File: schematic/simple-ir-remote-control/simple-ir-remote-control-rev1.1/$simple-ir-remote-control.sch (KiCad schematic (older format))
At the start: 24 parts, among them K1 CONN_3, P1 CONN_1, P2 CONN_1, P3 CONN_1, P4 CONN_1, P5 CONN_5, P6 CONN_4, P7 CONN_5X2, P8 CONN_10, P9 CONN_2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

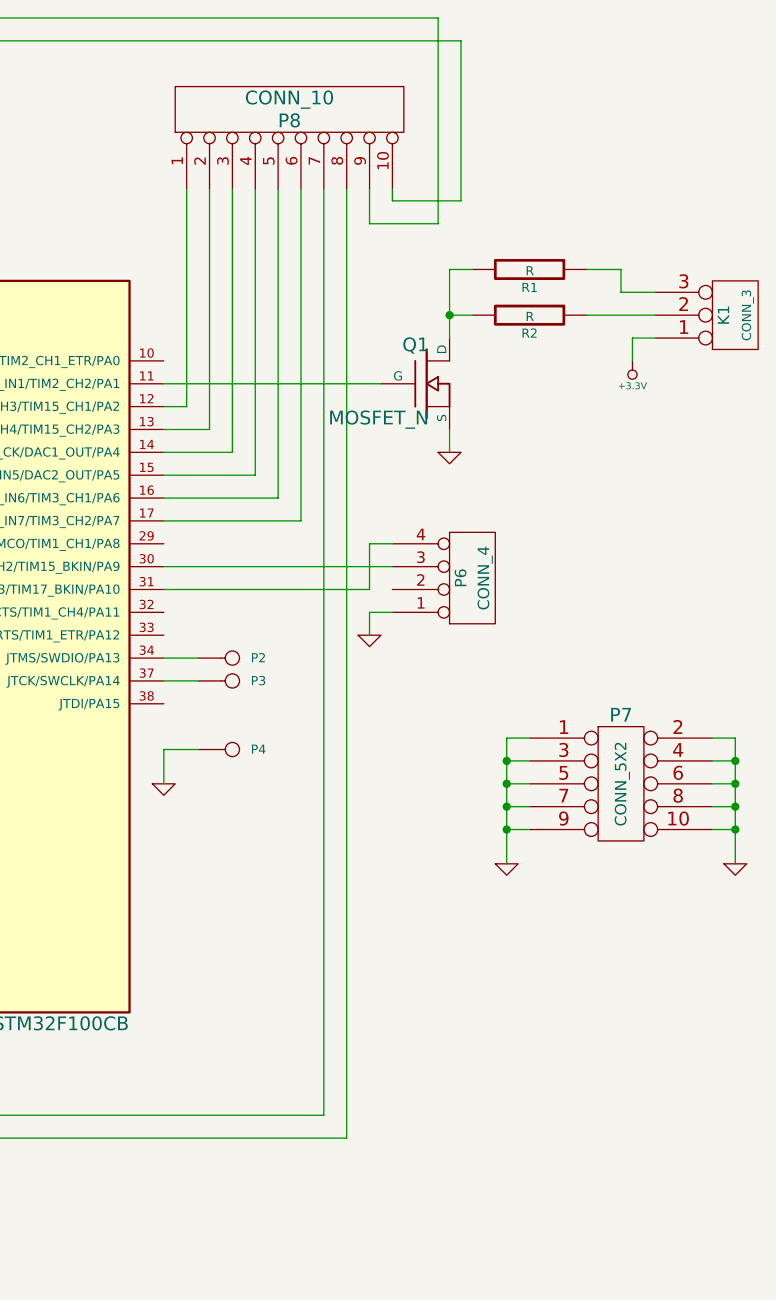
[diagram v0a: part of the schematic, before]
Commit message: Simple irrc rev 1.1 done - better design for manual producing
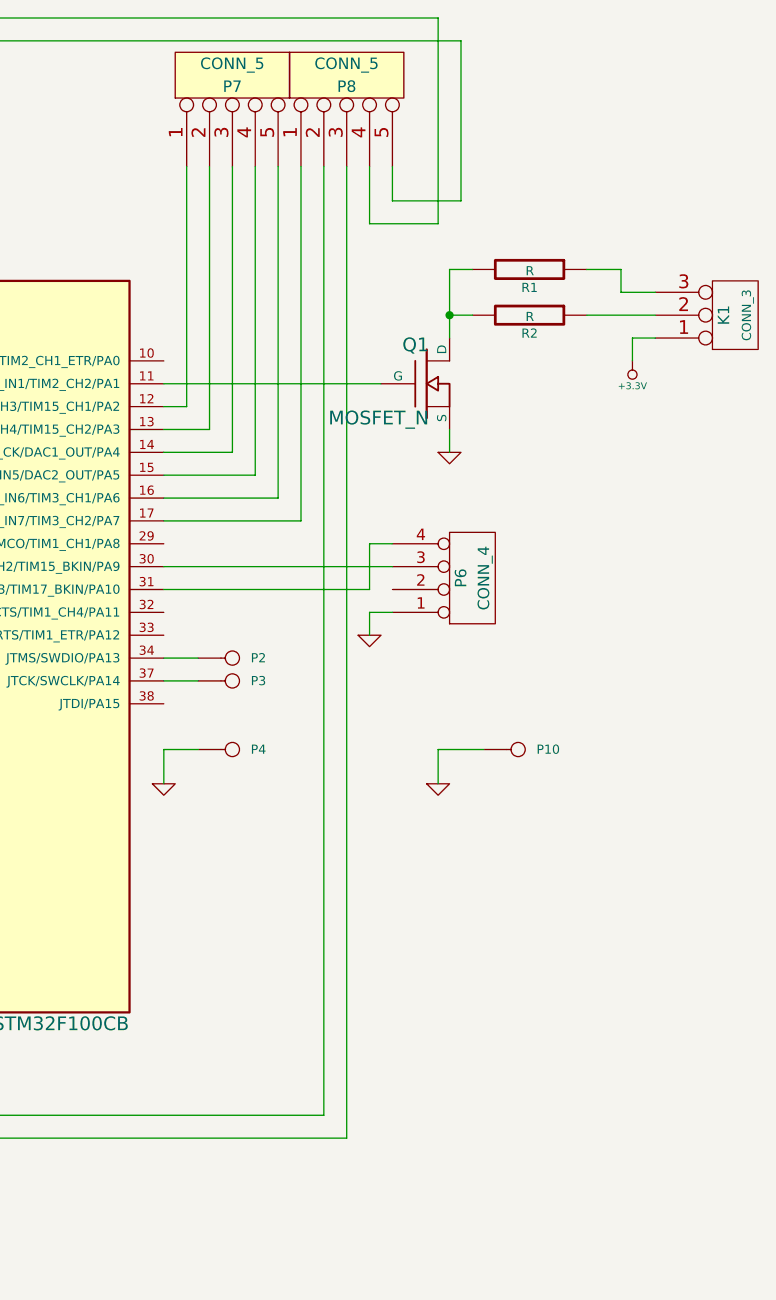
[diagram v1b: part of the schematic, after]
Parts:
- removed P7: CONN_5X2, ~, symbol CONN_5X2
- removed P8: CONN_10, ~, symbol CONN_10
- added P10: CONN_1, ~, symbol CONN_1
- added P7, P8: CONN_5, ~, symbol CONN_5
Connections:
- net GND: now also P10.1
- net at U2.12 (USART2_TX/ADC1_IN2/TIM2_CH3/TIM15_CH1/PA2): now also P7.1
- net at U2.13 (USART2_RX/ADC1_IN3/TIM2_CH4/TIM15_CH2/PA3): now also P7.2
- net at U2.14 (SPI1_NSS/ADC1_IN4/USART2_CK/DAC1_OUT/PA4): now also P7.3
- net at U2.15 (SPI1_SCK/ADC1_IN5/DAC2_OUT/PA5): now also P7.4
- net at U2.16 (SPI1_MISO/ADC1_IN6/TIM3_CH1/PA6): now also P7.5
- net at U2.17 (SPI1_MOSI/ADC1_IN7/TIM3_CH2/PA7): now also P8.1
- net at U2.18 (PB0/ADC1_IN8/TIM3_CH3): now also P8.2
- net at U2.19 (PB1/ADC1_IN9/TIM3_CH4): now also P8.3
- net at U2.20 (PB2/BOOT1): now also P8.4
- net at U2.21 (PB10/I2C2_SCL/USART3_TX): now also P8.5
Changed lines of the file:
@@
 LIBS:stm32
 LIBS:linStab-(1-GND,Adj,2-Out,3-in)
+LIBS:simple-ir-remote-control-cache
 EELAYER 27 0
 EELAYER END
@@
 Sheet 1 1
 Title ""
-Date "23 feb 2015"
+Date "28 feb 2015"
 Rev ""
 Comp ""
@@
 	7700 2500 7600 2500
 Wire Wire Line
-	7700 1550 7700 2500
-Wire Wire Line
-	7800 1550 7800 2600
+	7700 1450 7700 2500
+Wire Wire Line
+	7800 1450 7800 2600
 Wire Wire Line
 	7800 2600 7600 2600
@@
 	7900 2700 7600 2700
 Wire Wire Line
-	7900 1550 7900 2700
-Wire Wire Line
-	8000 1550 8000 2800
+	7900 1450 7900 2700
+Wire Wire Line
+	8000 1450 8000 2800
 Wire Wire Line
 	8000 2800 7600 2800
@@
 	8100 2900 7600 2900
 Wire Wire Line
-	8100 1550 8100 2900
-Wire Wire Line
-	8200 3000 7600 3000
-Wire Wire Line
-	8200 1550 8200 3000
+	8100 1450 8100 2900
 Wire Wire Line
 	4600 3400 3250 3400
@@
 	3350 3500 3350 5700
 $Comp
-L CONN_5X2 P7
-U 1 1 54EB6329
-P 9600 4150
-F 0 "P7" H 9600 4450 60  0000 C CNN
-F 1 "CONN_5X2" V 9600 4150 50  0000 C CNN
-F 2 "~" H 9600 4150 60  0000 C CNN
-F 3 "~" H 9600 4150 60  0000 C CNN
-	1    9600 4150
-	1    0    0    -1
-$EndComp
-$Comp
-L GND #PWR015
-U 1 1 54EB6338
-P 9100 4500
-F 0 "#PWR015" H 9100 4500 30  0001 C CNN
-F 1 "GND" H 9100 4430 30  0001 C CNN
-F 2 "" H 9100 4500 60  0000 C CNN
-F 3 "" H 9100 4500 60  0000 C CNN
-	1    9100 4500
-	1    0    0    -1
-$EndComp
-$Comp
-L GND #PWR016
-U 1 1 54EB6347
-P 10100 4500
-F 0 "#PWR016" H 10100 4500 30  0001 C CNN
-F 1 "GND" H 10100 4430 30  0001 C CNN
-F 2 "" H 10100 4500 60  0000 C CNN
-F 3 "" H 10100 4500 60  0000 C CNN
-	1    10100 4500
-	1    0    0    -1
-$EndComp
-Wire Wire Line
-	9100 4500 9100 3950
-Wire Wire Line
-	9100 3950 9200 3950
-Wire Wire Line
-	9200 4050 9100 4050
-Connection ~ 9100 4050
-Wire Wire Line
-	9200 4150 9100 4150
-Connection ~ 9100 4150
-Wire Wire Line
-	9200 4250 9100 4250
-Connection ~ 9100 4250
-Wire Wire Line
-	9200 4350 9100 4350
-Connection ~ 9100 4350
-Wire Wire Line
-	10000 3950 10100 3950
-Wire Wire Line
-	10100 3950 10100 4500
-Wire Wire Line
-	10000 4050 10100 4050
-Connection ~ 10100 4050
-Wire Wire Line
-	10000 4150 10100 4150
-Connection ~ 10100 4150
-Wire Wire Line
-	10000 4250 10100 4250
-Connection ~ 10100 4250
-Wire Wire Line
-	10000 4350 10100 4350
-Connection ~ 10100 4350
-$Comp
-L +3.3V #PWR017
+L +3.3V #PWR015
 U 1 1 54EB6839
 P 9650 2300
-F 0 "#PWR017" H 9650 2260 30  0001 C CNN
+F 0 "#PWR015" H 9650 2260 30  0001 C CNN
 F 1 "+3.3V" H 9650 2410 30  0000 C CNN
 F 2 "" H 9650 2300 60  0000 C CNN
@@
 Wire Wire Line
 	9650 2200 9650 2300
-$Comp
-L CONN_10 P8
-U 1 1 54EB7720
-P 8150 1200
-F 0 "P8" V 8100 1200 60  0000 C CNN
-F 1 "CONN_10" V 8200 1200 60  0000 C CNN
-F 2 "~" H 8150 1200 60  0000 C CNN
-F 3 "~" H 8150 1200 60  0000 C CNN
-	1    8150 1200
-	0    -1   -1   0
-$EndComp
 Wire Wire Line
 	4500 3600 4600 3600
@@
 $EndComp
 $Comp
-L GND #PWR018
+L GND #PWR016
 U 1 1 54EB81B9
 P 2000 4600
-F 0 "#PWR018" H 2000 4600 30  0001 C CNN
+F 0 "#PWR016" H 2000 4600 30  0001 C CNN
 F 1 "GND" H 2000 4530 30  0001 C CNN
 F 2 "" H 2000 4600 60  0000 C CNN
@@
 $EndComp
 $Comp
-L +BATT #PWR019
+L +BATT #PWR017
 U 1 1 54EB81C8
 P 2000 4150
-F 0 "#PWR019" H 2000 4100 20  0001 C CNN
+F 0 "#PWR017" H 2000 4100 20  0001 C CNN
 F 1 "+BATT" H 2000 4250 30  0000 C CNN
 F 2 "" H 2000 4150 60  0000 C CNN
@@
 	3250 5600 8300 5600
 Wire Wire Line
-	8300 5600 8300 1550
+	8300 5600 8300 1450
 Wire Wire Line
 	3350 5700 8400 5700
 Wire Wire Line
-	8400 5700 8400 1550
-Wire Wire Line
-	8500 1700 8500 1550
+	8400 5700 8400 1450
+Wire Wire Line
+	8500 1700 8500 1450
 Wire Wire Line
 	4600 4400 4400 4400
@@
 	8900 1600 8600 1600
 Wire Wire Line
-	8600 1600 8600 1550
+	8600 1600 8600 1450
+Wire Wire Line
+	8200 3000 7600 3000
+Wire Wire Line
+	8200 1450 8200 3000
+$Comp
+L CONN_5 P7
+U 1 1 54F18386
+P 7900 1050
+F 0 "P7" V 7850 1050 50  0000 C CNN
+F 1 "CONN_5" V 7950 1050 50  0000 C CNN
+F 2 "~" H 7900 1050 60  0000 C CNN
+F 3 "~" H 7900 1050 60  0000 C CNN
+	1    7900 1050
+	0    -1   -1   0
+$EndComp
+$Comp
+L CONN_5 P8
+U 1 1 54F18395
+P 8400 1050
+F 0 "P8" V 8350 1050 50  0000 C CNN
+F 1 "CONN_5" V 8450 1050 50  0000 C CNN
+F 2 "~" H 8400 1050 60  0000 C CNN
+F 3 "~" H 8400 1050 60  0000 C CNN
+	1    8400 1050
+	0    -1   -1   0
+$EndComp
+$Comp
+L CONN_1 P10
+U 1 1 54F1C7CE
+P 9150 4000
+F 0 "P10" H 9230 4000 40  0000 L CNN
+F 1 "CONN_1" H 9150 4055 30  0001 C CNN
+F 2 "~" H 9150 4000 60  0000 C CNN
+F 3 "~" H 9150 4000 60  0000 C CNN
+	1    9150 4000
+	1    0    0    -1
+$EndComp
+$Comp
+L GND #PWR018
+U 1 1 54F1C7DD
+P 8800 4150
+F 0 "#PWR018" H 8800 4150 30  0001 C CNN
+F 1 "GND" H 8800 4080 30  0001 C CNN
+F 2 "" H 8800 4150 60  0000 C CNN
+F 3 "" H 8800 4150 60  0000 C CNN
+	1    8800 4150
+	1    0    0    -1
+$EndComp
+Wire Wire Line
+	8800 4150 8800 4000
+Wire Wire Line
+	8800 4000 9000 4000
 $EndSCHEMATC
